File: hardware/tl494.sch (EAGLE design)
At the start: 91 parts, among them IC1 TL494CN, J1 CON_HEADER_1X02-PTH, J2 CON_HEADER_1X02-PTH, J3 J20MM, J4 J5MM, J5 J15MM, K2 24V, Q1 2N5551, Q1I 8050, Q1I1 2N3904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

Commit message: testing
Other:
- note added: "Original R18 is 470R 1W to 5K 1W"
- note removed: "Ic=15.1mA"
- note removed: "Ir=12mA (working)"
- note removed: "Ir=9mA(not working)"
- note removed: "Original R18 is 470R 1W to 2K 1W"
- note removed: "VGS 2.62V"
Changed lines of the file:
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@@
 to 4K 1/2W</text>
 <text x="134.62" y="33.02" size="1.778" layer="98">Original R18 is 470R 1W
-to 2K 1W</text>
+to 5K 1W</text>
 <text x="177.8" y="170.18" size="1.778" layer="98">Original R26 is 330R 1W
 to 560 + 560 1W</text>
@@
 <text x="106.68" y="96.52" size="1.778" layer="98" align="center">17mA</text>
 <text x="-2.54" y="-30.48" size="1.778" layer="98">108 Khz 3.2Vp-p</text>
-<text x="193.04" y="0" size="1.778" layer="98">VGS 2.62V</text>
 <text x="93.98" y="15.24" size="1.778" layer="98">Vr=17.44V</text>
 <text x="167.64" y="30.48" size="1.778" layer="98">Vr=31.19V</text>
 <text x="38.1" y="48.26" size="1.778" layer="98">350R Room Temp</text>
 <text x="210.82" y="165.1" size="1.778" layer="98">17mA diode current</text>
-<text x="86.36" y="12.7" size="1.778" layer="98">Ir=12mA (working)</text>
-<text x="86.36" y="10.16" size="1.778" layer="98">Ir=9mA(not working)</text>
 <text x="167.64" y="33.02" size="1.778" layer="98">Ir=17mA</text>
 <text x="170.18" y="53.34" size="1.778" layer="98">~48V</text>
@@
 R14=130k, R15=4.3k, I=357uA</text>
 <text x="93.98" y="-10.16" size="1.778" layer="98" align="center-left">Ib=188uA</text>
-<text x="109.22" y="2.54" size="1.778" layer="98" align="center-left">Ic=15.1mA</text>
 <text x="167.64" y="25.4" size="1.778" layer="98">Vr=7.08V</text>
 <text x="111.76" y="10.16" size="1.778" layer="98">Vr=15.66V</text>

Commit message: 1
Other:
- note added: "Bootstrap Capacitor"
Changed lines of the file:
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@@
 <text x="167.64" y="25.4" size="1.778" layer="98">Vr=7.08V</text>
 <text x="111.76" y="10.16" size="1.778" layer="98">Vr=15.66V</text>
+<text x="185.42" y="40.64" size="1.778" layer="98">Bootstrap
+Capacitor</text>
 </plain>
 <instances>

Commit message: 1
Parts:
- R15: value 4.3K -> 4.7K
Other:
- note added: "~35.3 wrt Q4s"
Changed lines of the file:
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@@
 <part name="C6" library="trosh_devices.eagle.v9" deviceset="CAPACITOR" device="C050-024X044_EXPAD" value="0.1uF"/>
 <part name="R14" library="trosh_devices.eagle.v9" deviceset="RESISTOR" device="0207/2V_EXPAD" value="130K"/>
-<part name="R15" library="trosh_devices.eagle.v9" deviceset="RESISTOR" device="0207/2V_EXPAD" value="4.3K"/>
+<part name="R15" library="trosh_devices.eagle.v9" deviceset="RESISTOR" device="0207/2V_EXPAD" value="4.7K"/>
 <part name="GND14" library="dp_devices.v6" deviceset="SUPPLY_GND" device=""/>
 <part name="Q1" library="dp_devices.v6" deviceset="TRANSISTOR_BJT_NPN" device="-TO-92-EBC" value="2N5551"/>
@@
 <text x="185.42" y="40.64" size="1.778" layer="98">Bootstrap
 Capacitor</text>
+<text x="165.1" y="38.1" size="1.778" layer="98">~35.3 wrt Q4s</text>
 </plain>
 <instances>

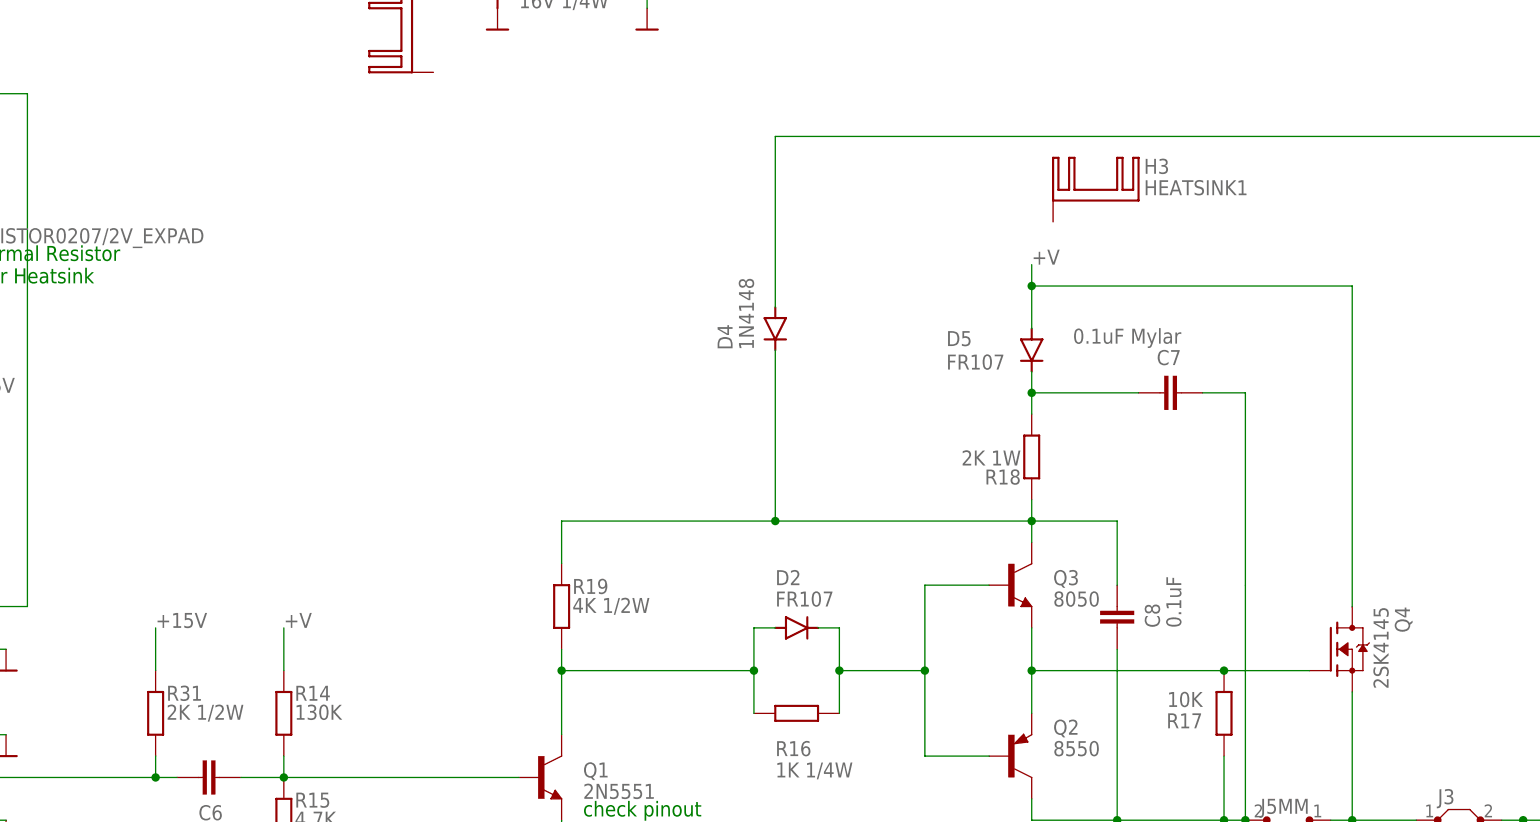
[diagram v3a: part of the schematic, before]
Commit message: new bootstrap circuit doc
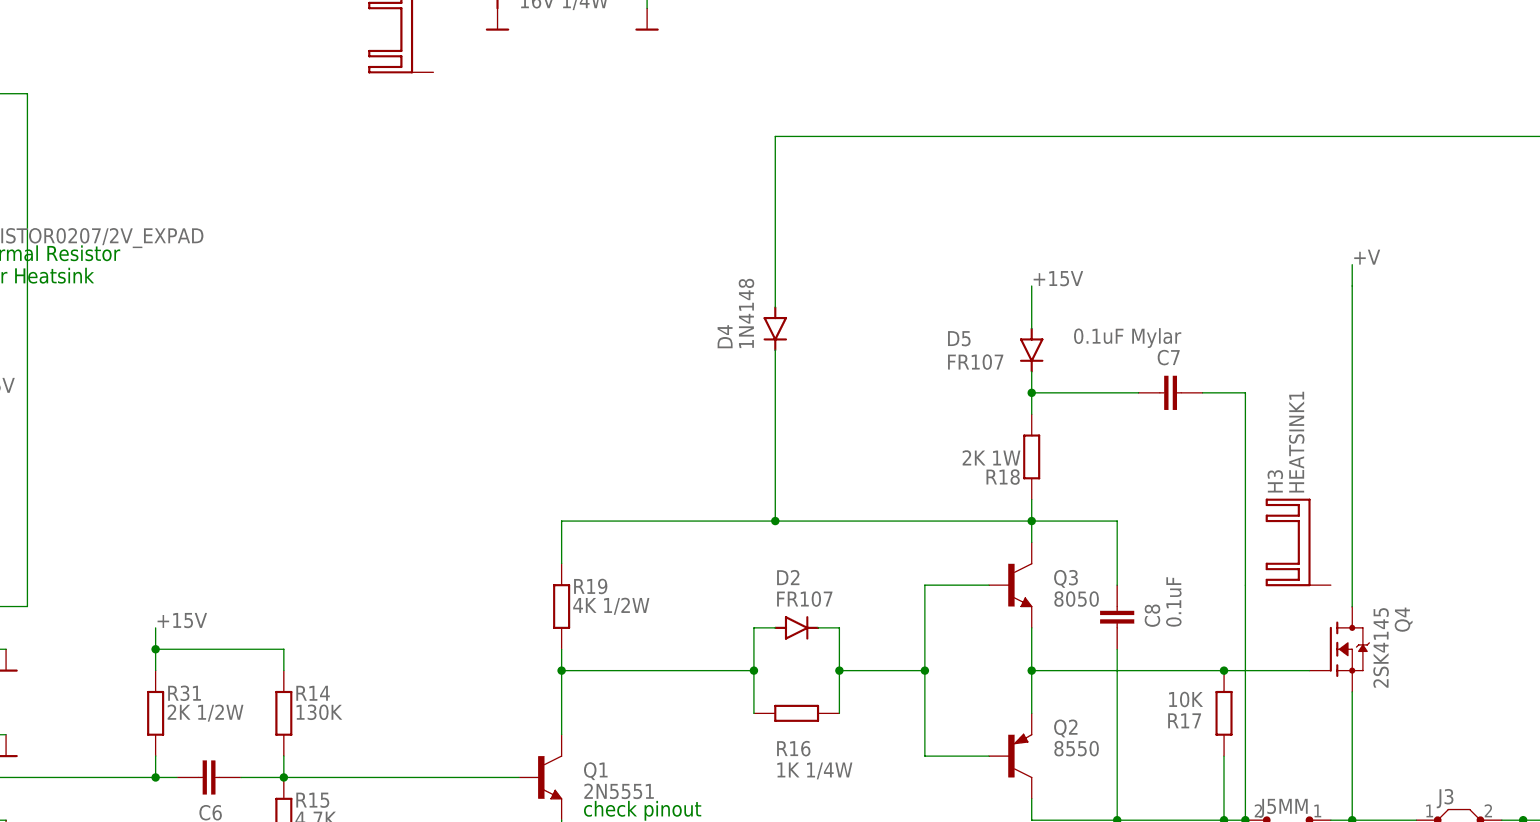
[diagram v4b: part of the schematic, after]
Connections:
- net +15V: now also D5.A, R14.2
- net +V: no longer D5.A, R14.2
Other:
- moved on the sheet: H3
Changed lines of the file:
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@@
 <?xml version="1.0" encoding="utf-8"?>
 <!DOCTYPE eagle SYSTEM "eagle.dtd">
-<eagle version="9.4.2">
+<eagle version="9.1.3">
 <drawing>
 <settings>
@@
 <text x="210.82" y="165.1" size="1.778" layer="98">17mA diode current</text>
 <text x="167.64" y="33.02" size="1.778" layer="98">Ir=17mA</text>
-<text x="170.18" y="53.34" size="1.778" layer="98">~48V</text>
+<text x="208.28" y="53.34" size="1.778" layer="98">~48V</text>
 <text x="71.12" y="-33.02" size="1.778" layer="98" align="center-left">Vdivider, V@R15
 @Vin 24V = 1.552V
@@
 <attribute name="VALUE" x="232.41" y="-16.002" size="1.778" layer="96"/>
 </instance>
-<instance part="H3" gate="G$1" x="172.72" y="60.96" smashed="yes">
-<attribute name="NAME" x="178.435" y="64.135" size="1.778" layer="95"/>
-<attribute name="VALUE" x="178.435" y="61.595" size="1.778" layer="96"/>
+<instance part="H3" gate="G$1" x="198.12" y="20.32" smashed="yes" rot="R90">
+<attribute name="NAME" x="194.945" y="26.035" size="1.778" layer="95" rot="R90"/>
+<attribute name="VALUE" x="197.485" y="26.035" size="1.778" layer="96" rot="R90"/>
 </instance>
 <instance part="H4" gate="G$1" x="223.52" y="-40.64" smashed="yes">
@@
 <segment>
 <pinref part="Q4" gate="Q" pin="D"/>
-<pinref part="D5" gate="1" pin="A"/>
-<wire x1="165.1" y1="45.72" x2="165.1" y2="50.8" width="0.1524" layer="91"/>
-<label x="165.1" y="53.34" size="1.778" layer="95"/>
-<wire x1="165.1" y1="50.8" x2="165.1" y2="53.34" width="0.1524" layer="91"/>
-<junction x="165.1" y="50.8"/>
-<wire x1="165.1" y1="50.8" x2="203.2" y2="50.8" width="0.1524" layer="91"/>
+<label x="203.2" y="53.34" size="1.778" layer="95"/>
+<wire x1="203.2" y1="50.8" x2="203.2" y2="53.34" width="0.1524" layer="91"/>
 <wire x1="203.2" y1="50.8" x2="203.2" y2="12.7" width="0.1524" layer="91"/>
-</segment>
-<segment>
-<pinref part="R14" gate="R" pin="2"/>
-<wire x1="76.2" y1="5.08" x2="76.2" y2="10.16" width="0.1524" layer="91"/>
-<label x="76.2" y="10.16" size="1.778" layer="95"/>
 </segment>
 <segment>
@@
 <segment>
 <pinref part="R31" gate="R" pin="2"/>
-<wire x1="60.96" y1="5.08" x2="60.96" y2="10.16" width="0.1524" layer="91"/>
+<wire x1="60.96" y1="5.08" x2="60.96" y2="7.62" width="0.1524" layer="91"/>
 <label x="60.96" y="10.16" size="1.778" layer="95"/>
-</segment>
-</net>
+<pinref part="R14" gate="R" pin="2"/>
+<wire x1="60.96" y1="7.62" x2="60.96" y2="10.16" width="0.1524" layer="91"/>
+<wire x1="76.2" y1="5.08" x2="76.2" y2="7.62" width="0.1524" layer="91"/>
+<wire x1="76.2" y1="7.62" x2="60.96" y2="7.62" width="0.1524" layer="91"/>
+<junction x="60.96" y="7.62"/>
+</segment>
+<segment>
+<pinref part="D5" gate="1" pin="A"/>
+<wire x1="165.1" y1="45.72" x2="165.1" y2="50.8" width="0.1524" layer="91"/>
+<label x="165.1" y="50.8" size="1.778" layer="95"/>
+</segment>
+</net>

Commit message: 1
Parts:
- R14: value 130K -> 68K
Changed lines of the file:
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@@
 <?xml version="1.0" encoding="utf-8"?>
 <!DOCTYPE eagle SYSTEM "eagle.dtd">
-<eagle version="9.1.3">
+<eagle version="9.4.2">
 <drawing>
 <settings>
@@
 <part name="R13" library="trosh_devices.eagle.v9" deviceset="RESISTOR" device="0207/2V_EXPAD" value="10K"/>
 <part name="C6" library="trosh_devices.eagle.v9" deviceset="CAPACITOR" device="C050-024X044_EXPAD" value="0.1uF"/>
-<part name="R14" library="trosh_devices.eagle.v9" deviceset="RESISTOR" device="0207/2V_EXPAD" value="130K"/>
+<part name="R14" library="trosh_devices.eagle.v9" deviceset="RESISTOR" device="0207/2V_EXPAD" value="68K"/>
 <part name="R15" library="trosh_devices.eagle.v9" deviceset="RESISTOR" device="0207/2V_EXPAD" value="4.7K"/>
 <part name="GND14" library="dp_devices.v6" deviceset="SUPPLY_GND" device=""/>

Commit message: 2
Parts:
- R18: value 2K 1W -> 470R 1W
- R19: value 4K 1/2W -> 1K 1/2W
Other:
- note added: "Vc=10V"
- note added: "Vc=3V"
- note added: "Vc=4V WRT Q4 source"
- note added: "calculated=2V"
- note removed: "Ir=17mA"
- note removed: "Original R18 is 470R 1W to 5K 1W"
- note removed: "Original R19 is 1K 1/2W to 4K 1/2W"
- note removed: "Vr=15.66V"
- note removed: "Vr=17.44V"
- note removed: "Vr=31.19V"
- note removed: "Vr=7.08V"
- note removed: "~35.3 wrt Q4s"
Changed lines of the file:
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@@
 <part name="GND16" library="dp_devices.v6" deviceset="SUPPLY_GND" device=""/>
 <part name="D4" library="trosh_devices.eagle.v9" deviceset="DIODE" device="DO35-20" value="1N4148"/>
-<part name="R18" library="trosh_devices.eagle.v9" deviceset="RESISTOR" device="0414V_EXPAD" value="2K 1W"/>
+<part name="R18" library="trosh_devices.eagle.v9" deviceset="RESISTOR" device="0414V_EXPAD" value="470R 1W"/>
 <part name="C7" library="trosh_devices.eagle.v9" deviceset="CAPACITOR" device="C050-050X075_EXPAD" value="0.1uF Mylar"/>
 <part name="D5" library="diode" library_urn="urn:adsk.eagle:library:210" deviceset="1N4933" device="" package3d_urn="urn:adsk.eagle:package:43336/1" value="FR107"/>
 <part name="C8" library="trosh_devices.eagle.v9" deviceset="CAPACITOR" device="C050-024X044_EXPAD" value="0.1uF"/>
-<part name="R19" library="trosh_devices.eagle.v9" deviceset="RESISTOR" device="0414V_EXPAD" value="4K 1/2W"/>
+<part name="R19" library="trosh_devices.eagle.v9" deviceset="RESISTOR" device="0414V_EXPAD" value="1K 1/2W"/>
 <part name="C9" library="trosh_devices.eagle.v9" deviceset="CAPACITOR" device="C050-024X044_EXPAD" value="0.1uF"/>
 <part name="GND17" library="dp_devices.v6" deviceset="SUPPLY_GND" device=""/>
@@
 Vout is 18V above</text>
 <text x="193.04" y="101.6" size="1.778" layer="98">Modified R29 to be 10K + 10K + 4.7K</text>
-<text x="101.6" y="25.4" size="1.778" layer="98">Original R19 is 1K 1/2W
-to 4K 1/2W</text>
-<text x="134.62" y="33.02" size="1.778" layer="98">Original R18 is 470R 1W
-to 5K 1W</text>
 <text x="177.8" y="170.18" size="1.778" layer="98">Original R26 is 330R 1W
 to 560 + 560 1W</text>
@@
 <text x="106.68" y="96.52" size="1.778" layer="98" align="center">17mA</text>
 <text x="-2.54" y="-30.48" size="1.778" layer="98">108 Khz 3.2Vp-p</text>
-<text x="93.98" y="15.24" size="1.778" layer="98">Vr=17.44V</text>
-<text x="167.64" y="30.48" size="1.778" layer="98">Vr=31.19V</text>
+<text x="111.76" y="2.54" size="1.778" layer="98">Vc=10V</text>
 <text x="38.1" y="48.26" size="1.778" layer="98">350R Room Temp</text>
 <text x="210.82" y="165.1" size="1.778" layer="98">17mA diode current</text>
-<text x="167.64" y="33.02" size="1.778" layer="98">Ir=17mA</text>
 <text x="208.28" y="53.34" size="1.778" layer="98">~48V</text>
 <text x="71.12" y="-33.02" size="1.778" layer="98" align="center-left">Vdivider, V@R15
@@
 R14=130k, R15=4.3k, I=357uA</text>
 <text x="93.98" y="-10.16" size="1.778" layer="98" align="center-left">Ib=188uA</text>
-<text x="167.64" y="25.4" size="1.778" layer="98">Vr=7.08V</text>
-<text x="111.76" y="10.16" size="1.778" layer="98">Vr=15.66V</text>
 <text x="185.42" y="40.64" size="1.778" layer="98">Bootstrap
 Capacitor</text>
-<text x="165.1" y="38.1" size="1.778" layer="98">~35.3 wrt Q4s</text>
+<text x="180.34" y="7.62" size="1.778" layer="98">Vc=3V</text>
+<text x="-81.28" y="30.48" size="1.778" layer="98">calculated=2V</text>
+<text x="144.78" y="38.1" size="1.778" layer="98">Vc=4V WRT Q4 source</text>
 </plain>
 <instances>
@@
 </instance>
 <instance part="C8" gate="G$1" x="175.26" y="12.7" smashed="yes">
-<attribute name="NAME" x="180.34" y="10.16" size="1.778" layer="95" rot="R90"/>
-<attribute name="VALUE" x="182.88" y="10.16" size="1.778" layer="96" rot="R90"/>
+<attribute name="NAME" x="177.8" y="15.24" size="1.778" layer="95"/>
+<attribute name="VALUE" x="177.8" y="12.7" size="1.778" layer="96"/>
 </instance>
 <instance part="R19" gate="R" x="109.22" y="12.7" smashed="yes" rot="R90">

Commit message: 1
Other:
- note added: "18 turns Ferrite Ring Black OD - 17.5mm ID - 9.5mm Thickness - 7mm Measured 29.04uH"
- note added: "Dual Diode Peak Repetitive Reverse Voltage: 60V"
- note removed: "18 turns Ferrite Ring Black OD - 17.5mm ID - 9.5mm Thickness - 7mm"
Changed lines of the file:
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@@
 OD - 17.5mm
 ID - 9.5mm
-Thickness - 7mm</text>
+Thickness - 7mm
+Measured 29.04uH</text>
 <text x="210.82" y="236.22" size="1.778" layer="98">SW</text>
 <text x="241.3" y="208.28" size="1.778" layer="98">Latch circuit</text>
@@
 <text x="-81.28" y="30.48" size="1.778" layer="98">calculated=2V</text>
 <text x="144.78" y="38.1" size="1.778" layer="98">Vc=4V WRT Q4 source</text>
+<text x="175.26" y="-22.86" size="1.778" layer="98">Dual Diode
+Peak Repetitive Reverse Voltage: 60V</text>
 </plain>
 <instances>

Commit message: 1
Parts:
- added C18: 100uF 25V, trosh_devices.eagle.v9:CAPACITOR-POLE2,5-7_EXPAD
- added D6: 13V 1/4W, diode:BZV10
- added J6, J7, J8: J5MM, jumper:J5MM
- added Q7: 2N3904, dp_devices.v6:TRANSISTOR_BJT_NPN-TO-92-EBC
- added R23: 10K, trosh_devices.eagle.v9:RESISTOR0207/2V_EXPAD
- added R24: 470R 1W, trosh_devices.eagle.v9:RESISTOR0414V_EXPAD
- C16: value 100uF 25V -> 10uF 50V
- D10: value 16V 1/4W -> 21V 1/4W
- D2: value FR107 -> RGP15J; device trosh_devices.eagle.v9:DIODEDO41-2.5V -> diode:1N4933
- D3: value FCH30A06 -> FCHS20A08
- D4: value 1N4148 -> FR107; device trosh_devices.eagle.v9:DIODEDO35-20 -> diode:1N4933
- R19: value 1K 1/2W -> 1K 5W
- R33: value 100K -> 10K
- renumbered Q1I to Q8, Q1I1 to Q10, Q2I to Q9
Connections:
- removed net +15V: C16.+, C4.2, D5.A, IC1.VCC, Q5.E, R14.2, R31.2
- removed net +V: C10.+, C11.+, C9.1, K22.P, Q4.D, Q5.C, R33.1
- new net +12.4V: C4.2, D4.C, IC1.VCC, R24.1, R31.2
- new net +21.6V: C16.+, D5.A, Q5.E, R14.2
- new net +48V: C10.+, C11.+, C9.1, J7.1, K22.P, Q4.D, Q5.C, R33.1
- new net N$40: D6.C, Q7.B, R23.2
- new net N$41: C18.+, Q7.E, R24.2
- new net N$42: D5.C, J6.1
- new net N$43: J7.2, Q7.C, R23.1
- new net N$44: D4.A, J8.2
- net GND: now also C18.-, D6.A
- net N$18: no longer D4.C
- net N$19: now also J6.2; no longer D5.C
- net VOUT: now also J8.1; no longer D4.A
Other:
- note added: "Changes: 2/1/2020 R33 from 100k to 10k D10 from 16V to 22.2V Zener 16V+6.2V C16 from 100uF 25V to 10uF 50V Remove D4 R19 from 1/2W to 5W Q4 from 2SK4145 to FQPF50N06 D3 from FCH30A06 to FCHS20A08 D5 & D2 from FR107 to RGP15J New Q1I2 - 2N3904 R23 10K R24 470R 1/2W D6 13V Zener C18 - 100uF 25V D4 - FR107"
- note added: "Switching MOSFET Supply"
- note removed: "17mA diode current"
- note removed: "48V Input MOD circuit"
- note removed: "Original R26 is 330R 1W to 560 + 560 1W"
- note removed: "Vc=4V WRT Q4 source"
- note removed: "~48V"
- moved on the sheet: D4, D5, H1, H2, H3, H4, H5, J5
